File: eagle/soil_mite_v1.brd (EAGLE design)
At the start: 100 x 80 mm, 23 parts

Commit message: updated files. need to understand new components
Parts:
- added JP1: (no value), pinhead:2X05
- added JP2: (no value), pinhead:2X03
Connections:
- new net N$1: JP1.1
- new net N$6: JP1.2
- new net P0.01: JP1.3, U$1.5
- new net P0.03: JP1.5, U$1.7
- new net P0.04: JP1.6, U$1.8
- new net P0.05: JP1.7, U$1.9
- new net VREADY: JP2.2, U$1.48
- net +1V8: now also JP2.3
- net FROMSOIL_CAP: now also JP1.4
- net GND: now also JP1.10, JP2.4
- net SOIL_PWM: now also JP1.9; no longer U$1.5
- net TEMP_EN: now also JP1.8
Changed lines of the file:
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@@
 <?xml version="1.0" encoding="utf-8"?>
 <!DOCTYPE eagle SYSTEM "eagle.dtd">
-<eagle version="6.5.0">
+<eagle version="6.6.0">
 <drawing>
 <settings>
@@
 <layers>
 <layer number="1" name="Top" color="4" fill="1" visible="yes" active="yes"/>
+<layer number="2" name="Route2" color="1" fill="3" visible="no" active="no"/>
+<layer number="3" name="Route3" color="4" fill="3" visible="no" active="no"/>
+<layer number="4" name="Route4" color="1" fill="4" visible="no" active="no"/>
+<layer number="5" name="Route5" color="4" fill="4" visible="no" active="no"/>
+<layer number="6" name="Route6" color="1" fill="8" visible="no" active="no"/>
+<layer number="7" name="Route7" color="4" fill="8" visible="no" active="no"/>
+<layer number="8" name="Route8" color="1" fill="2" visible="no" active="no"/>
+<layer number="9" name="Route9" color="4" fill="2" visible="no" active="no"/>
+<layer number="10" name="Route10" color="1" fill="7" visible="no" active="no"/>
+<layer number="11" name="Route11" color="4" fill="7" visible="no" active="no"/>
+<layer number="12" name="Route12" color="1" fill="5" visible="no" active="no"/>
+<layer number="13" name="Route13" color="4" fill="5" visible="no" active="no"/>
+<layer number="14" name="Route14" color="1" fill="6" visible="no" active="no"/>
+<layer number="15" name="Route15" color="4" fill="6" visible="no" active="no"/>
 <layer number="16" name="Bottom" color="1" fill="1" visible="yes" active="yes"/>
 <layer number="17" name="Pads" color="2" fill="1" visible="yes" active="yes"/>
@@
 <element name="C12" library="SparkFun-Capacitors" package="0402-CAP" value=".01uF" x="34.29" y="12.7"/>
 <element name="U$5" library="soil_monitor" package="SOT353" value="TRISTATE_BUFFER_SOT353" x="66.04" y="30.48"/>
+<element name="JP1" library="pinhead" package="2X05" value="" x="7.62" y="-5.08"/>
+<element name="JP2" library="pinhead" package="2X03" value="" x="-5.08" y="-5.08"/>
 </elements>
 <signals>
@@
 <contactref element="U$4" pad="5"/>
 <contactref element="U$5" pad="3"/>
+<contactref element="JP2" pad="4"/>
+<contactref element="JP1" pad="10"/>
 <wire x1="45.974" y1="57.546" x2="44.244378125" y2="59.89561875" width="0" layer="19" extent="1-1"/>
 <wire x1="44.704" y1="55.895" x2="45.974" y2="57.546" width="0" layer="19" extent="1-1"/>
@@
 <wire x1="36.385" y1="20.32" x2="56.2" y2="30.48" width="0" layer="19" extent="1-1"/>
 <wire x1="33.64" y1="12.7" x2="36.385" y2="20.32" width="0" layer="19" extent="1-1"/>
+<wire x1="12.7" y1="-3.81" x2="33.64" y2="12.7" width="0" layer="19" extent="1-1"/>
+<wire x1="-5.08" y1="-3.81" x2="12.7" y2="-3.81" width="0" layer="19" extent="1-1"/>
 </signal>
 <signal name="N$2">
@@
 <signal name="+1V8">
 <contactref element="C7" pad="1"/>
-<contactref element="U$1" pad="1"/>
-<contactref element="C11" pad="1"/>
 <contactref element="U$1" pad="12"/>
 <contactref element="C10" pad="1"/>
@@
 <contactref element="U$5" pad="5"/>
 <contactref element="U$5" pad="2"/>
+<contactref element="JP2" pad="3"/>
+<contactref element="U$1" pad="1"/>
+<contactref element="C11" pad="1"/>
 <wire x1="42.54" y1="53" x2="44.704" y2="54.595" width="0" layer="19" extent="1-1"/>
 <wire x1="42.54" y1="52.6" x2="42.54" y2="53" width="0" layer="19" extent="1-1"/>
@@
 <wire x1="65.09" y1="30.48" x2="45.974" y2="46.34" width="0" layer="19" extent="1-1"/>
 <wire x1="66.99" y1="31.13" x2="65.09" y2="30.48" width="0" layer="19" extent="1-1"/>
+<wire x1="-5.08" y1="-6.35" x2="34.798" y2="48.275" width="0" layer="19" extent="1-1"/>
 </signal>
 <signal name="FROMSOIL_CAP">
 <contactref element="U$1" pad="6"/>
 <contactref element="R2" pad="2"/>
+<contactref element="JP1" pad="4"/>
 <wire x1="56.73" y1="17.78" x2="36.2" y2="51" width="0" layer="19" extent="1-1"/>
+<wire x1="5.08" y1="-3.81" x2="56.73" y2="17.78" width="0" layer="19" extent="1-1"/>
 </signal>
 <signal name="SOIL_PWM">
 <contactref element="U$3" pad="OUT"/>
 <contactref element="U$1" pad="4"/>
-<contactref element="U$1" pad="5"/>
-<wire x1="36.2" y1="51.4" x2="36.2" y2="51.8" width="0" layer="19" extent="1-1"/>
-<wire x1="13.97" y1="12.7" x2="36.2" y2="51.4" width="0" layer="19" extent="1-1"/>
+<contactref element="JP1" pad="9"/>
+<wire x1="13.97" y1="12.7" x2="36.2" y2="51.8" width="0" layer="19" extent="1-1"/>
+<wire x1="12.7" y1="-6.35" x2="13.97" y2="12.7" width="0" layer="19" extent="1-1"/>
 </signal>
 <signal name="N$5">
@@
 <contactref element="U$5" pad="1"/>
 <contactref element="U$1" pad="10"/>
+<contactref element="JP1" pad="8"/>
 <wire x1="36.2" y1="49.4" x2="65.09" y2="31.13" width="0" layer="19" extent="1-1"/>
+<wire x1="10.16" y1="-3.81" x2="36.2" y2="49.4" width="0" layer="19" extent="1-1"/>
 </signal>
 <signal name="TRISTATE">
@@
 <wire x1="34.94" y1="12.7" x2="58.1" y2="29.83" width="0" layer="19" extent="1-1"/>
 </signal>
+<signal name="N$1">
+<contactref element="JP1" pad="1"/>
+</signal>
+<signal name="N$6">
+<contactref element="JP1" pad="2"/>
+</signal>
+<signal name="P0.01">
+<contactref element="JP1" pad="3"/>
+<contactref element="U$1" pad="5"/>
+<wire x1="5.08" y1="-6.35" x2="36.2" y2="51.4" width="0" layer="19" extent="1-1"/>
+</signal>
+<signal name="P0.03">
+<contactref element="JP1" pad="5"/>
+<contactref element="U$1" pad="7"/>
+<wire x1="7.62" y1="-6.35" x2="36.2" y2="50.6" width="0" layer="19" extent="1-1"/>
+</signal>
+<signal name="P0.05">
+<contactref element="JP1" pad="7"/>
+<contactref element="U$1" pad="9"/>
+<wire x1="10.16" y1="-6.35" x2="36.2" y2="49.8" width="0" layer="19" extent="1-1"/>
+</signal>
+<signal name="P0.04">
+<contactref element="JP1" pad="6"/>
+<contactref element="U$1" pad="8"/>
+<wire x1="7.62" y1="-3.81" x2="36.2" y2="50.2" width="0" layer="19" extent="1-1"/>
+</signal>
+<signal name="VREADY">
+<contactref element="U$1" pad="48"/>
+<contactref element="JP2" pad="2"/>
+<wire x1="-7.62" y1="-3.81" x2="37.17" y2="53.97" width="0" layer="19" extent="1-1"/>
+</signal>
 </signals>

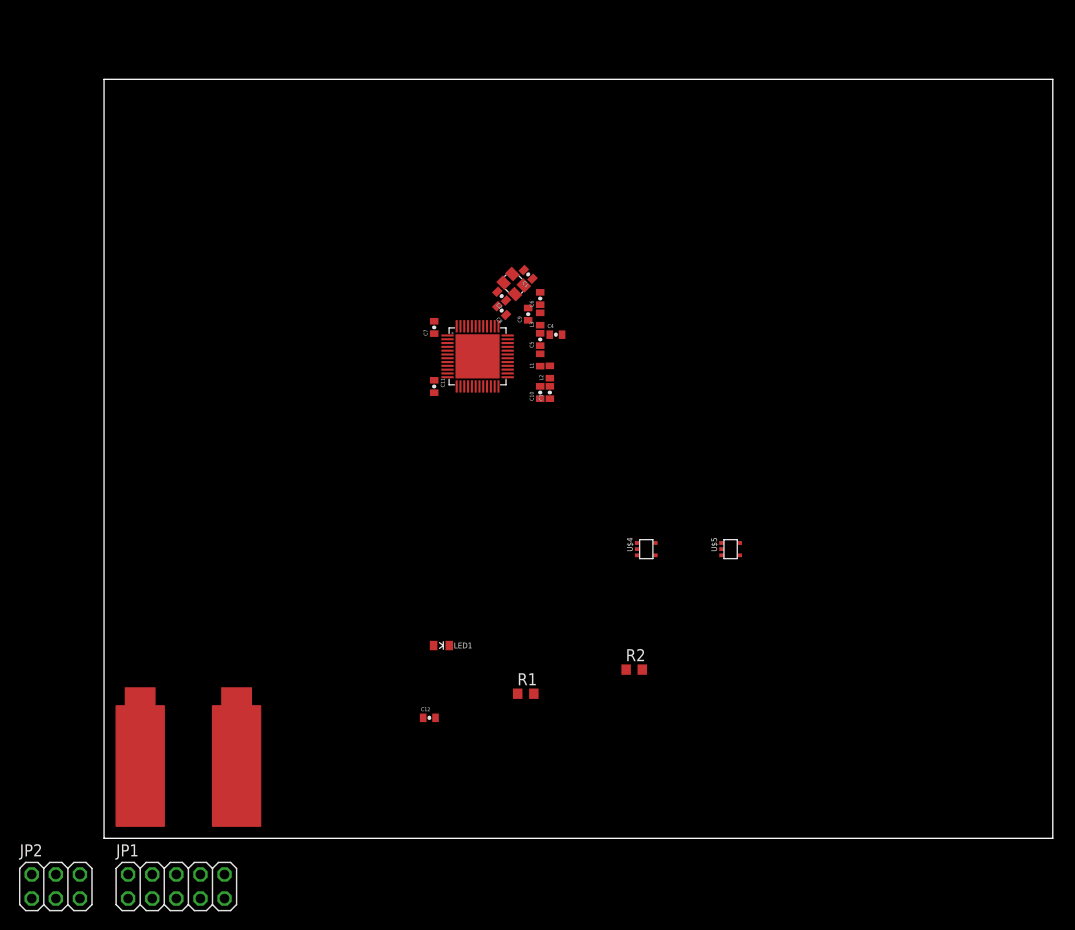
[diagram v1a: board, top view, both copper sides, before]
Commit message: need to route board. 'layout' part done. need eagle professional to finish
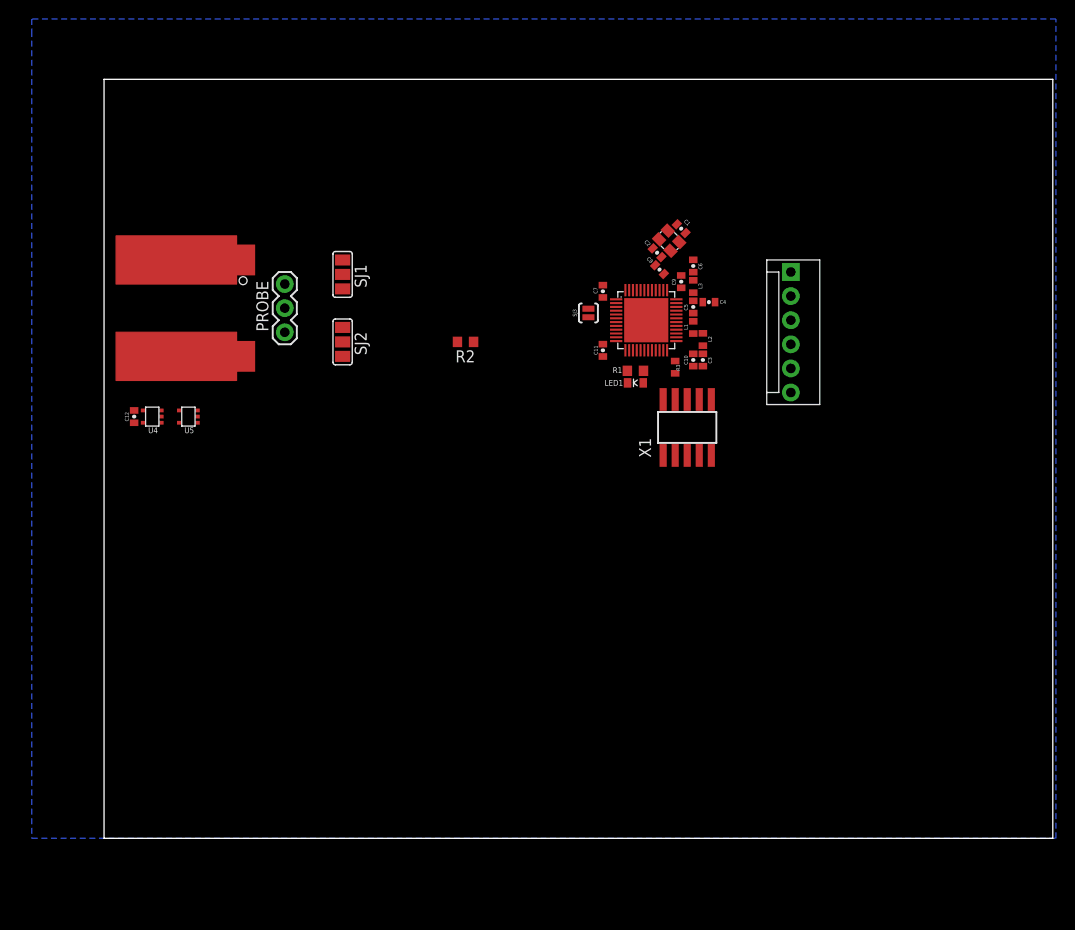
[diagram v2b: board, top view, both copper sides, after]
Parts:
- removed JP1: (no value), pinhead:2X05
- removed JP2: (no value), pinhead:2X03
- removed U$4: TEMP_SENSOR_LMT84, soil_monitor:SOT353
- removed U$5: TRISTATE_BUFFER_SOT353, soil_monitor:SOT353
- added JP3: (no value), SparkFun-Connectors:MOLEX-1X6
- added PROBE: (no value), SparkFun-Connectors:1X03
- added R3: 12k, MAAV_13v1:RCL_R0402
- added SJ1, SJ2: (no value), SparkFun-Passives:SJ_2
- added SJ3: SOLDERJUMPERNO, SparkFun-Passives:SJ_2S-NO
- added U4: TEMP_SENSOR_LMT84, soil_monitor:SOT353
- added U5: TRISTATE_BUFFER_SOT353, soil_monitor:SOT353
- added X1: 1365-10, con-leotronics:1365-10
- U$3: value SOIL_PROBE_TOP_TOP -> SOIL_PROBE_TOP_TOPOUT-IN; device soil_monitor:PROBE_LAYOUT_1 -> soil_monitor:PROBE_LAYOUT_1_OUT-IN
- moved U$3 48.3 mm to (7.62, 55.9), turned to 270 degrees
- moved C12 44.5 mm to (3.17, 44.5), turned to 90 degrees
- moved R2 38.9 mm to (38.1, 52.3), turned to 180 degrees
- moved R1 35.9 mm to (56.0, 49.3), turned to 180 degrees
- moved LED1 34.4 mm to (56.0, 48.0), turned to 180 degrees
- moved C11 18.2 mm to (52.6, 51.4)
- moved C7 18.2 mm to (52.6, 57.7)
- moved U$1 18.2 mm to (57.1, 54.6)
- moved C8 17.2 mm to (58.5, 59.9), turned to 315 degrees
- moved C2 17.0 mm to (58.3, 61.7)
- moved U$2 17.0 mm to (59.6, 63.0)
- moved C1 16.8 mm to (60.8, 64.3), turned to 315 degrees
- moved C10 16.5 mm to (62.1, 50.4)
- moved C5 16.5 mm to (62.1, 56.0)
- moved C6 16.5 mm to (62.1, 60.3)
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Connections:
- removed net N$1: JP1.1
- removed net N$3: R2.1, U$3.IN
- removed net N$6: JP1.2
- removed net P0.01: JP1.3, U$1.5
- removed net P0.03: JP1.5, U$1.7
- removed net P0.04: JP1.6, U$1.8
- removed net P0.05: JP1.7, U$1.9
- new net FROMSOIL_CAP_JUNC1: SJ2.3, U$3.IN
- new net FROMSOIL_CAP_JUNC2: PROBE.3, SJ2.1
- new net SOIL_PWM_JUNC1: SJ1.3, U$3.OUT
- new net SOIL_PWM_JUNC2: PROBE.1, SJ1.1
- new net SWDCLK: R3.2, U$1.24, X1.4
- new net SWDIO: U$1.23, X1.2
- new net TOSOIL_CAP: SJ3.2, U$1.5
- net +1V8: now also JP3.2, U5.2, U5.5; no longer JP2.3, U$5.2, U$5.5
- net FROMSOIL_CAP: now also R2.1, SJ2.2; no longer JP1.4
- net GND: now also JP3.4, R3.1, U4.1, U4.2, U4.5, U5.3, X1.3, X1.5, X1.9; no longer JP1.10, JP2.4, U$4.1, U$4.2, U$4.5, U$5.3
- net SOIL_PWM: now also SJ1.2, SJ3.1; no longer JP1.9, U$3.OUT
- net TEMP: now also U4.3; no longer U$4.3
- net TEMP_EN: now also U5.1; no longer JP1.8, U$5.1
- net TRISTATE: now also U4.4, U5.4; no longer U$4.4, U$5.4
- net VREADY: now also JP3.6; no longer JP2.2
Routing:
- added copper zone on layer 16, net N$1

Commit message: finished layout. let me know if there are glaring errors
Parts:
- added J$1: SMA_EDGE, SparkFun-Connectors:SMA-EDGE
- moved C9 46.5 mm to (89.3, 21.8)
- moved R2 46.5 mm to (68.4, 17.0)
- moved L2 46.3 mm to (91.6, 16.0), turned to 270 degrees
- moved C10 46.3 mm to (90.6, 13.8), turned to 270 degrees
- moved C3 46.3 mm to (91.6, 13.8), turned to 270 degrees
- moved C5 46.3 mm to (90.8, 19.7)
- moved C6 46.3 mm to (90.8, 24.0)
- moved C1 46.3 mm to (89.5, 27.9)
- moved L3 46.3 mm to (90.8, 21.8)
- moved U$2 46.2 mm to (88.0, 26.5), turned to 45 degrees
- moved C4 46.2 mm to (92.5, 20.3)
- moved C11 46.2 mm to (80.8, 14.9)
- moved C7 46.2 mm to (80.8, 21.1)
- moved SJ3 46.2 mm to (79.2, 18.8)
- moved C2 46.2 mm to (86.5, 25.1)
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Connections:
- net ANTENNA: now also J$1.SIG
- net GND: now also J$1.GND@0, J$1.GND@1, J$1.GND@2, J$1.GND@3
- net XC1: now also U$2.X2; no longer U$2.X1
- net XC2: now also U$2.X1; no longer U$2.X2
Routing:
- net +1V8: track 0.00 -> 93.9 mm, vias 0 -> 5
- net TEMP: track 0.00 -> 78.2 mm
- net TEMP_EN: track 0.00 -> 77.8 mm
- net SOIL_PWM_JUNC1: track 0.00 -> 40.4 mm
- net FROMSOIL_CAP_JUNC1: track 0.00 -> 40.4 mm
- net SOIL_PWM: track 0.00 -> 30.9 mm
- net FROMSOIL_CAP: track 0.00 -> 27.6 mm
- net GND: track 0.00 -> 17.1 mm, vias 0 -> 7
- net VREADY: track 0.00 -> 11.0 mm
- net INDICATOR: track 0.00 -> 8.85 mm
- net XC1: track 0.00 -> 7.49 mm
- net SWDCLK: track 0.00 -> 7.10 mm
- net ANTENNA: track 0.00 -> 6.70 mm
- net FROMSOIL_CAP_JUNC2: track 0.00 -> 6.31 mm
- net SOIL_PWM_JUNC2: track 0.00 -> 6.31 mm
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- added copper zone on layer 16, net +1V8
- added copper zone on layer 1, net GND
- added copper zone on layer 16, net GND
- removed copper zone on layer 16, net N$1
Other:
- board size 100 x 80 mm -> 99.2 x 33.6 mm

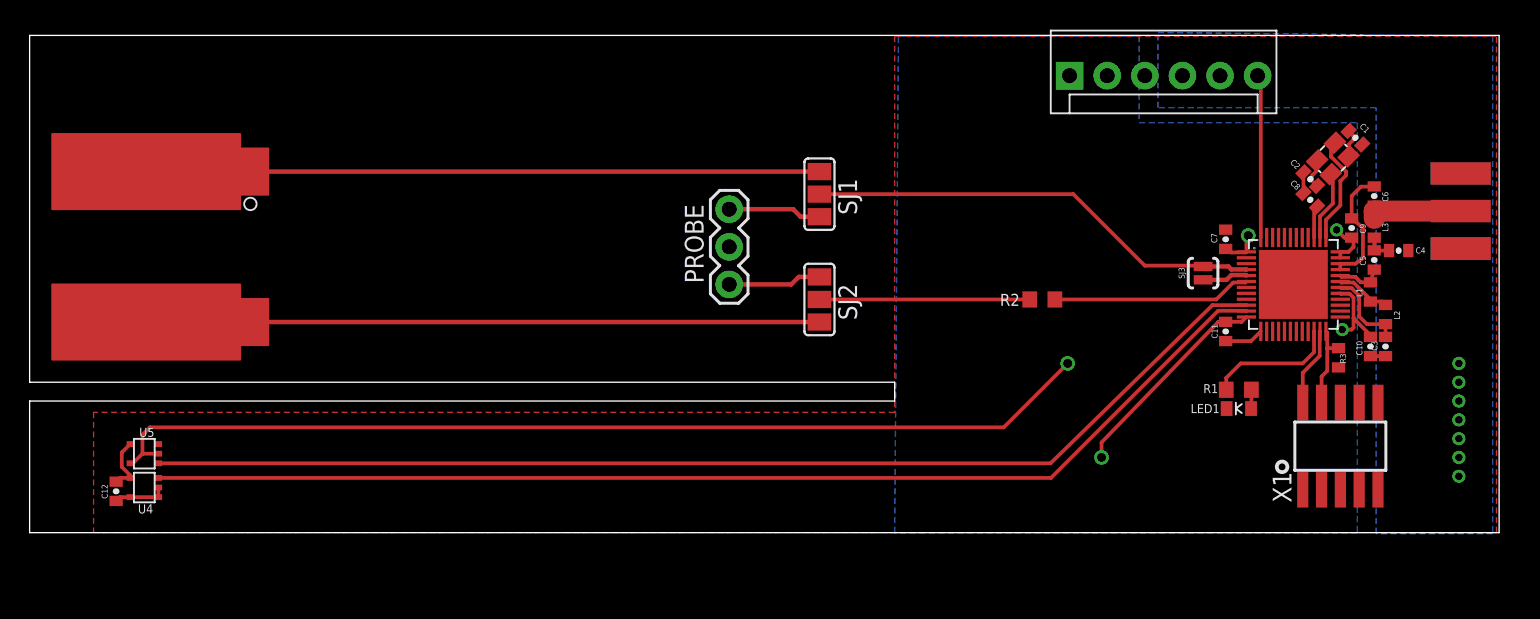
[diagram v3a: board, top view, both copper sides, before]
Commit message: finalized soil mite design. sending out for shipping
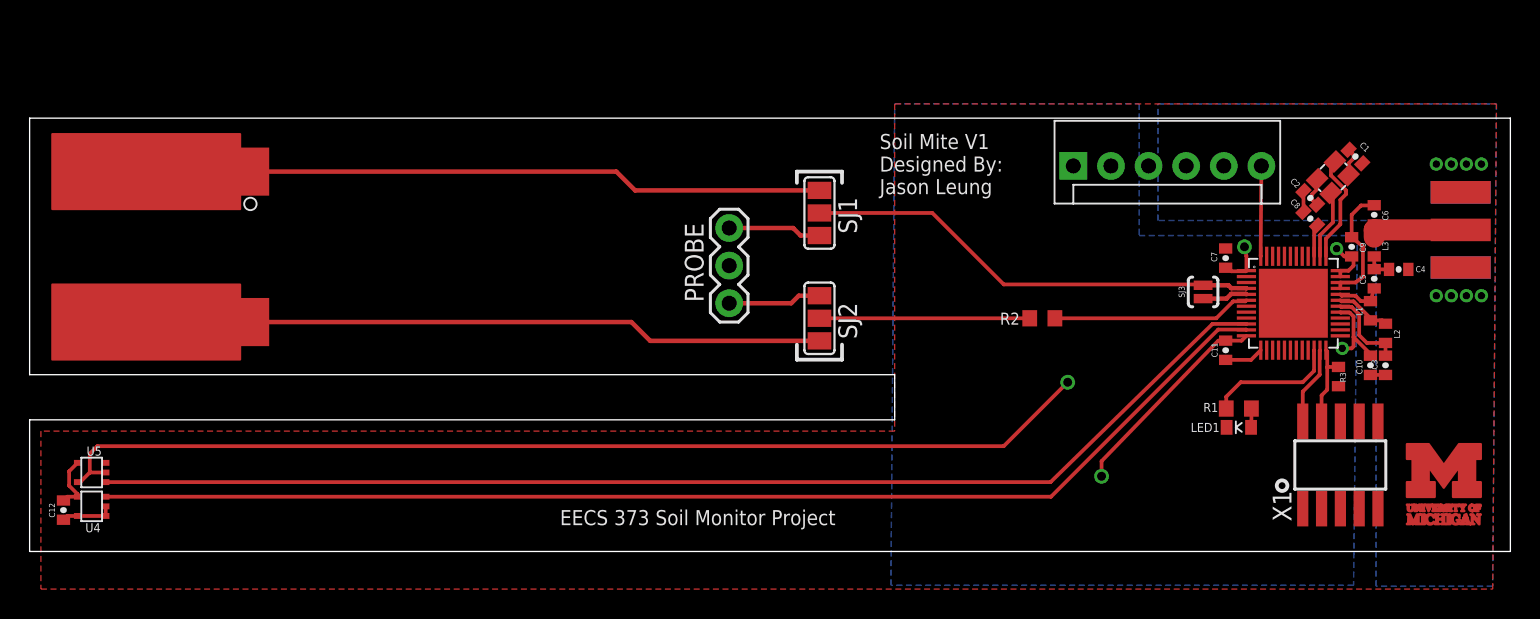
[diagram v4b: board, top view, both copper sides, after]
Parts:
- added U$5: (no value), BlockM:BLOCK-M-DOUBLE-STACKED-5MM_MASK
- moved JP3 6.10 mm to (70.5, 26.0)
- moved U4 3.78 mm to (4.19, 3.05)
- moved U5 3.78 mm to (4.19, 5.33)
- moved C12 3.78 mm to (2.29, 2.79)
- moved R1 1.27 mm to (81.7, 9.65)
- moved R2 1.27 mm to (68.4, 15.7)
- moved SJ2 1.27 mm to (53.3, 15.7)
- moved X1 1.27 mm to (88.5, 5.84)
- moved C1 1.27 mm to (89.5, 26.7)
- moved C10 1.27 mm to (90.6, 12.6)
- moved C11 1.27 mm to (80.8, 13.6)
- moved C2 1.27 mm to (86.5, 23.9)
- moved C3 1.27 mm to (91.6, 12.6)
- moved C4 1.27 mm to (92.5, 19.1)
- moved C5 1.27 mm to (90.8, 18.4)
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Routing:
- net VREADY: track 11.0 -> 6.10 mm
- net +1V8: track 93.9 -> 97.9 mm
- net TEMP_EN: track 77.8 -> 81.4 mm
- net TEMP: track 78.2 -> 81.7 mm
- net SOIL_PWM_JUNC1: track 40.4 -> 40.9 mm
- net FROMSOIL_CAP_JUNC1: track 40.4 -> 40.9 mm
- net GND: vias 7 -> 8
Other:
- board size 99.2 x 33.6 mm -> 100 x 29.3 mm
- board text added: "EECS 373 Soil Monitor Project"
- board text added: "Soil Mite V1 Designed By: Jason Leung"
